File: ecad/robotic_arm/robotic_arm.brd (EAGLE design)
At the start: 81.3 x 61 mm, 118 parts, among them J1 (ID,OD)=(2.1,5.5)MM, SW1 5A/28V, Y1 16MHz

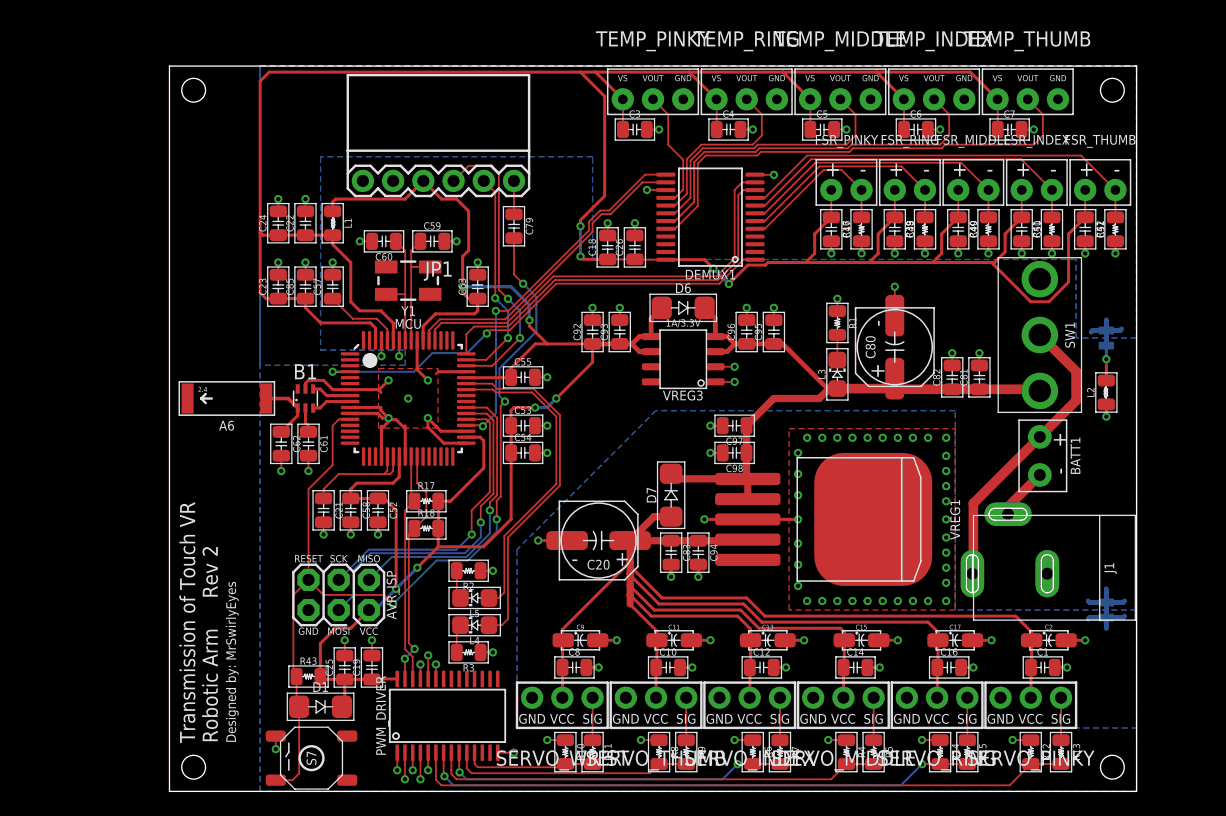
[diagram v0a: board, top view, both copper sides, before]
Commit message: Replaced Robotic Arm components for those with 3D models.  Also went down to 0402 component size.
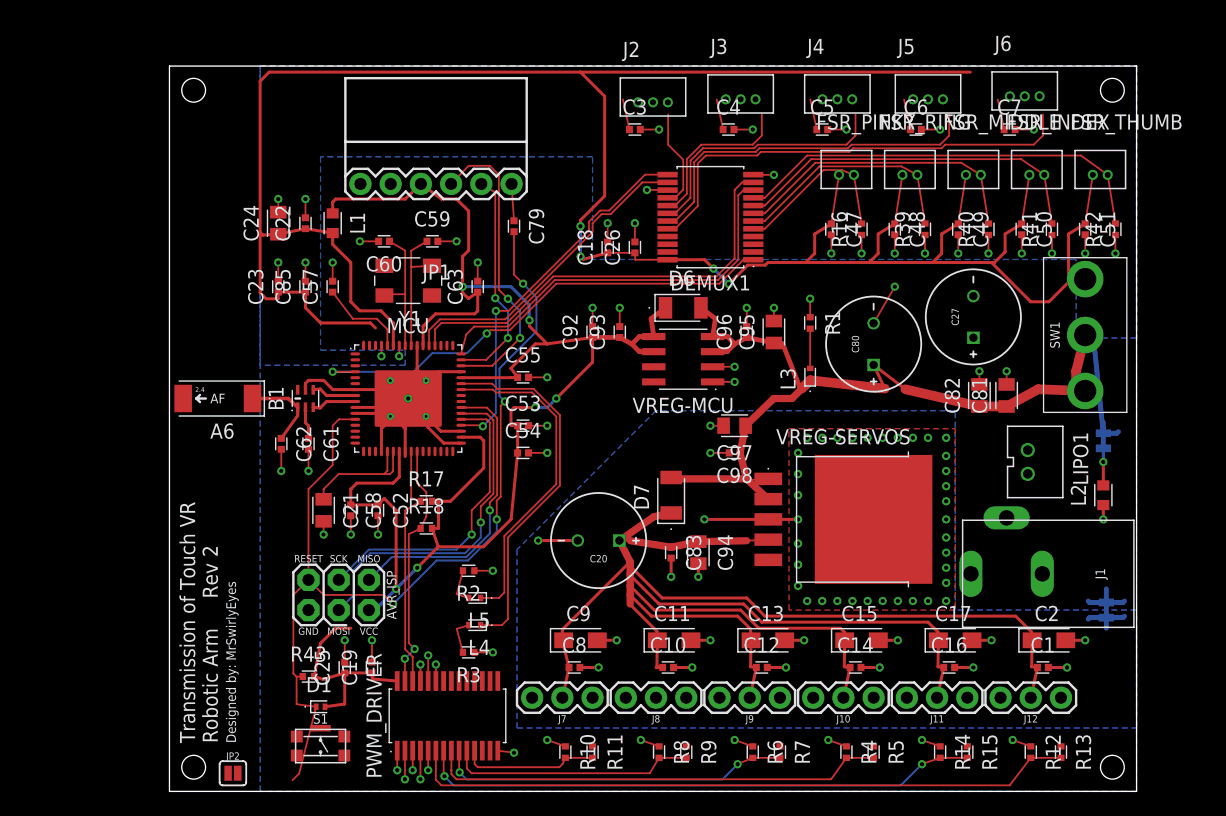
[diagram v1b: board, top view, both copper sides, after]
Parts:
- removed BATT1: BATTERYPTH_HOLES, PiB:DUAL_PTH_PADS
- removed S7: TACTILE-SW_500mA/12V, PiB_switches:BTN_MOMENTARY_SPST-NO_SMD_12V_50MA_L5.2-W5.2
- removed SERVO_INDEX, SERVO_MIDDLE, SERVO_PINKY, SERVO_RING, SERVO_THUMB, SERVO_WRIST: HK15298B, PiB:CONNECTOR_SERVO
- removed TEMP_INDEX, TEMP_MIDDLE, TEMP_PINKY, TEMP_RING, TEMP_THUMB: TMP36, PiB:CONNECTOR_TMP36
- removed VREG1: 5A/5V, PiB_ic_power:TO-263-5
- removed VREG3: 1A/3.3V, PiB_ic_power:SOIC-8_W3.9MM
- added C27: 1000uF/16V, PiB_capacitors:_AE_PTH_DIA8-LS3.5-H21.50
- added J10, J11, J12, J7, J8, J9: HK15298B, PiB_motors:1X03-VERT-MALE
- added J2, J3, J4, J5, J6: (no value), PiB_connectors:_MOLEX-0530470310_VERT_PITCH-1.25MM
- added JP2: JUMPER-SMT_2_NO_SILK, PiB_connectors:SMT-JUMPER_2_NO_SILK
- added LIPO1: Molex VERT 2mm pitch, PiB_batteries:BATTERY_MOLEX-89400_VERT_PITCH-2MM
- added S1: 50mA/32V, PiB_switches:BTN_MOMENTARY_SPDT-NO_L4.6-W2.8
- added VREG-MCU: 1A/3.3V, PiB_ic_power:SOIC127P600X265-8
- added VREG-SERVOS: 5A/5V, PiB_ic_power:TO170P1363X457-6
- A6: value 2.4GHz/802.11/0.5dBi/3W -> 2.45GHz; device PiB_radio_frequency:ANTENNA-CHIP5 -> PiB_radio_frequency:ANTC6522X100
- AVR_ISP: value AVR ISP -> AVRISP
- B1: value Impedence UNBAL/BAL (50Ω/100Ω) -> 50/100; device PiB_radio_frequency:0805_BALUN -> PiB_radio_frequency:RESCAXE65P200X125X95-6
- C1, C10, C12, C14, C16, C19, C22, C23, C26, C3, C4, C47, C48, C49, C5, C50, C51, C52, C53, C54, C55, C57, C58, C6, C63, C7, C79, C8, C83, C85, C93, C96, C98: device PiB_capacitors:_CER_SMD-805 -> PiB_capacitors:CAPC1005X55_SMD-0402
- C11, C13, C15, C17, C2, C9: value 10uF/20V -> 10uF/16V; device PiB_capacitors:_TANT_SMD-1206 -> PiB_capacitors:CAPMP3216X180_SMD_CAP-TANT-1206
- C18, C25, C92: value 10uF/25V -> 10uF/6.3V; device PiB_capacitors:_CER_SMD-805 -> PiB_capacitors:CAPC1005X55_SMD-0402
- C20: value 100UF/16V -> 1000uF/16V; device PiB_capacitors:_AE_SMD_L6.6-W6.6 -> PiB_capacitors:_AE_PTH_DIA8-LS3.5-H21.50
- C21, C24, C82, C94, C95, C97: device PiB_capacitors:_CER_SMD-805 -> PiB_capacitors:CAPC2012X95_SMD-0805
- C59, C60: value 12pF/250V -> 12pF/100V; device PiB_capacitors:_CER_SMD-805 -> PiB_capacitors:CAPC1005X55_SMD-0402
- C61: value 22PF/250V -> 22pF/100V; device PiB_capacitors:_CER_SMD-805 -> PiB_capacitors:CAPC1005X55_SMD-0402
- C62: value 0.75PF/100V -> 0.75pF/50V; device PiB_capacitors:_CER_SMD-805 -> PiB_capacitors:CAPC1005X55_SMD-0402
- C80: value 220uF/16V -> 1000uF/16V; device PiB_capacitors:_AE_SMD_L6.6-W6.6 -> PiB_capacitors:_AE_PTH_DIA8-LS3.5-H21.50
- C81: value 0.1uF/50V -> 0.1uF/35V; device PiB_capacitors:_CER_SMD-805 -> PiB_capacitors:CAPC2012X95_SMD-0805
- D1: value 1A/50V -> 150mA/75V; device PiB_discrete_semiconductors:SOD123F -> PiB_discrete_semiconductors:DFN100X60X55-2
- D6, D7: device PiB_discrete_semiconductors:SOD123F -> PiB_discrete_semiconductors:SODFL3516X170
- DEMUX1: device PiB:SSOP-24 -> PiB:SOP65P780X200-24
- FSR_INDEX, FSR_MIDDLE, FSR_PINKY, FSR_RING, FSR_THUMB: value FSR -> 10K; device PiB:CONNECTOR_FSR -> PiB_sensors:_MOLEX-0530470210_VERT_PITCH-1.25MM
- J1: value (ID,OD)=(2.1,5.5)MM -> 5A/28V; device PiB_connectors:POWER_JACK_SLOT_ID2.1MM-OD5.5MM -> PiB_connectors:POWER_JACK_PTH_ID2.1MM-OD5.5MM
- JP1: value FTDIPTH-RA -> FTDI
- L1, L2: value 10uH -> 10uH/380mA; device PiB_inductors:_SMD-805 -> PiB_inductors:INDC1608X60
- L3, L4, L5: device PiB_leds:LED_SMD-805_ -> PiB_leds:LEDC1005X40
- MCU: value ATMEGA128RFA1 -> ATMEGA128RFA1_VFQFN-64_NO-EXPOSED-PAD; device PiB_ic_microcontrollers:VFQFN-64 -> PiB_ic_microcontrollers:QFN50P900X900X90-64
- PWM_DRIVER: device PiB:TSSOP-28 -> PiB:SOP65P650X110-28
- R1, R10, R12, R14, R16, R39, R4, R40, R41, R42, R43, R6, R8: value 10KΩ -> 10K; device PiB_resistors:RESISTOR_SMD-805 -> PiB_resistors:RESC1005X35_SMD-0402
- R11, R13, R15, R5, R7, R9: value 100Ω -> 100; device PiB_resistors:RESISTOR_SMD-805 -> PiB_resistors:RESC1005X35_SMD-0402
- R17, R18: value 4.7K -> 10K; device PiB_resistors:RESISTOR_SMD-805 -> PiB_resistors:RESC1005X35_SMD-0402
- R2: value 2KΩ -> 1K; device PiB_resistors:RESISTOR_SMD-805 -> PiB_resistors:RESC1005X35_SMD-0402
- R3: value 1KΩ -> 1K; device PiB_resistors:RESISTOR_SMD-805 -> PiB_resistors:RESC1005X35_SMD-0402
- Y1: value 16MHz -> 16 MHz; device PiB:CRYSTAL-SMD-5X3 -> PiB:OSCCC500X320X110
- moved ANALOG_BR 8.64 mm to (81.0, 26.9)
- moved L2 8.64 mm to (81.0, 22.4)
- moved JP1 6.61 mm to (24.9, 48.5), turned to 90 degrees
- moved SW1 3.81 mm to (79.5, 35.8), turned to 0 degrees
- moved J1 3.34 mm to (72.9, 15.7)
- moved C81 2.75 mm to (72.9, 30.7)
- moved C82 2.75 mm to (70.6, 30.7)
- moved L3 2.29 mm to (56.4, 32.5)
- moved R1 2.29 mm to (56.4, 36.8)
- moved C80 1.80 mm to (61.7, 35.1)
- moved A6 0.76 mm to (6.60, 30.5)
- turned B1 to 90 degrees
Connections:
- removed net BATT_+: BATT1.+, J1.PWR, SW1.2
- removed net BATT_-: BATT1.-, J1.GND@2
- new net +: J1.PWR, LIPO1.+, SW1.P
- new net -: J1.GND@1, LIPO1.-
- new net N$12: JP2.2, MCU.62
- net 5V: now also C11.A, C13.A, C15.A, C17.A, C2.A, C20.+, C9.A, J10.VCC, J11.VCC, J12.VCC, J7.VCC, J8.VCC, J9.VCC, VREG-SERVOS.4; no longer C11.+, C13.+, C15.+, C17.+, C2.+, C20.A, C9.+, SERVO_INDEX.2, SERVO_MIDDLE.2, SERVO_PINKY.2, SERVO_RING.2, SERVO_THUMB.2, SERVO_WRIST.2, VREG1.4
- net AGND: now also J2.1, J3.1, J4.1, J5.1, J6.1, MCU.EP, MCU.P$1, MCU.P$2, MCU.P$3, MCU.P$4, MCU.P$5; no longer TEMP_INDEX.3, TEMP_MIDDLE.3, TEMP_PINKY.3, TEMP_RING.3, TEMP_THUMB.3
- net AVCC: now also FSR_INDEX.1, FSR_MIDDLE.1, FSR_PINKY.1, FSR_RING.1, FSR_THUMB.1, J2.3, J3.3, J4.3, J5.3, J6.3, JP2.1; no longer FSR_INDEX.+, FSR_MIDDLE.+, FSR_PINKY.+, FSR_RING.+, FSR_THUMB.+, MCU.62, TEMP_INDEX.1, TEMP_MIDDLE.1, TEMP_PINKY.1, TEMP_RING.1, TEMP_THUMB.1
- net FSR_INDEX: now also FSR_RING.2; no longer FSR_RING.-
- net FSR_MIDDLE: now also FSR_MIDDLE.2; no longer FSR_MIDDLE.-
- net FSR_PINKY: now also FSR_THUMB.2; no longer FSR_THUMB.-
- net FSR_RING: now also FSR_INDEX.2; no longer FSR_INDEX.-
- net FSR_THUMB: now also FSR_PINKY.2; no longer FSR_PINKY.-
- net GND: now also AVR_ISP.GND, C27.-, C80.-, J1.GND@2, S1.2, VREG-MCU.1, VREG-MCU.2; no longer AVR_ISP.6, C80.K, J1.GND@1, S7.1, VREG3.1, VREG3.2
- net MISO: now also AVR_ISP.MISO; no longer AVR_ISP.1
- net MOSI: now also AVR_ISP.MOSI; no longer AVR_ISP.4
- net N$1: now also J7.SIG; no longer SERVO_WRIST.1
- net N$39: now also A6.1; no longer A6.FEED
- net N$4: now also J8.SIG; no longer SERVO_THUMB.1
- net N$6: now also J9.SIG; no longer SERVO_INDEX.1
- net N$7: now also J10.SIG; no longer SERVO_MIDDLE.1
- net N$8: now also J11.SIG; no longer SERVO_RING.1
- net N$9: now also J12.SIG; no longer SERVO_PINKY.1
- net NGND: now also C11.K, C13.K, C15.K, C17.K, C2.K, C20.-, C9.K, J10.GND, J11.GND, J12.GND, J7.GND, J8.GND, J9.GND, VREG-SERVOS.3, VREG-SERVOS.6; no longer C11.-, C13.-, C15.-, C17.-, C2.-, C20.K, C9.-, SERVO_INDEX.3, SERVO_MIDDLE.3, SERVO_PINKY.3, SERVO_RING.3, SERVO_THUMB.3, SERVO_WRIST.3, VREG1.3, VREG1.TAB
- net RESET: now also AVR_ISP.RESET, S1.3; no longer AVR_ISP.5, S7.3
- net SCK: now also AVR_ISP.SCK; no longer AVR_ISP.3
- net TEMP_INDEX: now also J3.2; no longer TEMP_RING.2
- net TEMP_MIDDLE: now also J4.2; no longer TEMP_MIDDLE.2
- net TEMP_PINKY: now also J6.2; no longer TEMP_THUMB.2
- net TEMP_RING: now also J5.2; no longer TEMP_INDEX.2
- net TEMP_THUMB: now also J2.2; no longer TEMP_PINKY.2
- net VBATT: now also C27.+, C80.+, SW1.S1, VREG-MCU.3, VREG-MCU.4, VREG-SERVOS.1, VREG-SERVOS.2; no longer C80.A, SW1.1, VREG1.1, VREG1.2, VREG3.3, VREG3.4
- net VCC: now also VREG-MCU.5, VREG-MCU.6; no longer AVR_ISP.2, VREG3.5, VREG3.6
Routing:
- net BATT_+: track 24.9 -> 0.00 mm
- net AGND: track 31.0 -> 48.8 mm
- net GND: track 99.3 -> 109.7 mm, vias 48 -> 43
- net VBATT: track 56.3 -> 66.3 mm
- net VCC: track 144.0 -> 151.3 mm
- net AVCC: track 235.9 -> 228.8 mm
- net +: track 0.00 -> 5.61 mm
- net NGND: track 34.3 -> 39.9 mm
- net BATT_-: track 4.40 -> 0.00 mm
- net 5V: track 159.8 -> 163.7 mm
- net N$9: track 3.57 -> 0.00 mm
- net N$8: track 3.57 -> 0.00 mm
- net N$7: track 3.57 -> 0.00 mm
- net N$6: track 3.57 -> 0.00 mm
- net N$4: track 3.57 -> 0.00 mm
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- removed copper zone on layer 1, net GND

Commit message: Start on Rev 2 of robotic arm.  Made minor fixes to Touch Glove Rev 2.
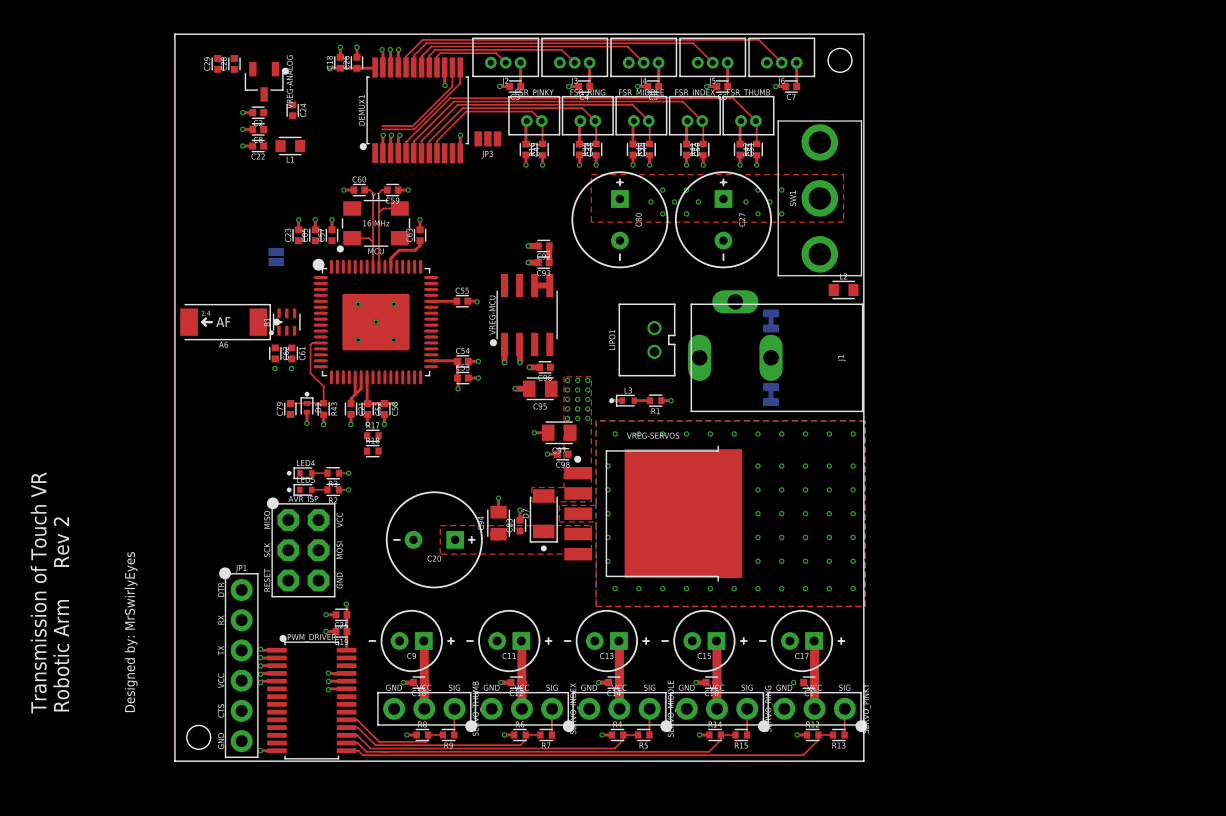
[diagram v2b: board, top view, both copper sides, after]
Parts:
- removed ANALOG_BR: 2PT_GND_TIE, PiB_power_symbols:2PT_GND_TIE
- removed C81: 0.1uF/35V, PiB_capacitors:CAPC2012X95_SMD-0805
- removed C82: 10uF/25V, PiB_capacitors:CAPC2012X95_SMD-0805
- removed D6: 1A/50V, PiB_discrete_semiconductors:SODFL3516X170
- removed J10, J11, J12, J7, J8, J9: HK15298B, PiB_motors:1X03-VERT-MALE
- removed L4: GREEN, PiB_leds:LEDC1005X40
- removed L5: RED, PiB_leds:LEDC1005X40
- removed R10: 10K, PiB_resistors:RESC1005X35_SMD-0402
- removed R11: 100, PiB_resistors:RESC1005X35_SMD-0402
- removed S1: 50mA/32V, PiB_switches:BTN_MOMENTARY_SPDT-NO_L4.6-W2.8
- added C28: 0.1uF/50V, PiB_capacitors:CAPC1005X55_SMD-0402
- added C29: 10uF/6.3V, PiB_capacitors:CAPC1005X55_SMD-0402
- added JP3: JUMPER_SMD_3-PAD_NO_NO-SILK, PiB_connectors:SMT-JUMPER_3_NO_NO-SILK
- added LED4: GREEN, PiB_leds:LEDC1005X40_LED-0402
- added LED5: RED, PiB_leds:LEDC1005X40_LED-0402
- added NOISE_BR1: NET_BRIDGE, PiB_power_symbols:NET_BRIDGE
- added SERVO_INDEX, SERVO_MIDDLE, SERVO_PINKY, SERVO_RING, SERVO_THUMB: HK15298B, PiB_motors:HDRV3W64P254_1X3_762X254X838B
- added VREG-ANALOG: MCP1700-1802 1.8V/200mA, PiB_ic_power:SOT95P237X112-3_SOT-23-3
- AVR_ISP: value AVRISP -> PTH VERT MALE; device PiB_connectors:2X3-NS -> PiB_connectors:HDRV6W64P254_2X3_762X483X838B_AVR-ISP
- C11, C13, C15, C17, C9: value 10uF/16V -> (none); device PiB_capacitors:CAPMP3216X180_SMD_CAP-TANT-1206 -> PiB_capacitors:_AE_PTH-DIA5-LS2-H11
- C2: value 10uF/16V -> 0.1uF/50V; device PiB_capacitors:CAPMP3216X180_SMD_CAP-TANT-1206 -> PiB_capacitors:CAPC1005X55_SMD-0402
- C21: device PiB_capacitors:CAPC2012X95_SMD-0805 -> PiB_capacitors:CAPC1005X55_SMD-0402
- C24: value 1uF/25V -> 0.1uF/50V; device PiB_capacitors:CAPC2012X95_SMD-0805 -> PiB_capacitors:CAPC1005X55_SMD-0402
- C8: value 0.1uF/50V -> 10uF/6.3V
- JP1: device PiB_connectors:FTDI_BASIC-6PIN-MALE-RA -> PiB_connectors:HDRV6W64P254_1X6_1524X254X838B_FTDI
- JP2: value JUMPER-SMT_2_NO_SILK -> JUMPER_SMD_2-PAD_NO_SILK
- L1, L2: device PiB_inductors:INDC1608X60 -> PiB_inductors:INDC1608X60-0603
- L3: device PiB_leds:LEDC1005X40 -> PiB_leds:LEDC1005X40_LED-0402
- LIPO1: value Molex VERT 2mm pitch -> 7.4V
- MCU: value ATMEGA128RFA1_VFQFN-64_NO-EXPOSED-PAD -> ATMEGA128RFA1
- NOISE_BR: value 2PT_GND_TIE -> NET_BRIDGE; device PiB_power_symbols:2PT_GND_TIE -> PiB_power_symbols:NET_BRIDGE
- Y1: device PiB:OSCCC500X320X110 -> PiB_crystals_oscillators_resonators:OSCCC500X320X110_CRYSTAL
- moved C2 79.9 mm to (10.0, 54.5), turned to 180 degrees
- moved C8 52.5 mm to (10.0, 53.1), turned to 180 degrees
- moved JP2 43.5 mm to (11.5, 42.4), flipped to the bottom, turned to 270 degrees
- moved JP1 37.8 mm to (8.61, 14.4), turned to 270 degrees
- moved NOISE_BR 33.5 mm to (53.1, 30.8)
- moved LIPO1 33.0 mm to (43.3, 35.4), turned to 90 degrees
- moved R42 30.9 mm to (51.9, 51.4)
- moved R41 30.1 mm to (47.4, 51.4)
- moved FSR_THUMB 29.9 mm to (51.2, 53.8)
- moved C51 29.8 mm to (50.5, 51.4)
- moved R40 29.3 mm to (42.9, 51.4)
- moved J1 29.1 mm to (50.1, 33.9)
- moved FSR_INDEX 29.1 mm to (46.7, 53.8)
- moved C50 29.0 mm to (46.0, 51.4)
- moved R39 28.4 mm to (38.4, 51.4)
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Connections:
- removed net C10: DEMUX1.21
- removed net C5: DEMUX1.4
- removed net C6: DEMUX1.3
- removed net C7: DEMUX1.2
- removed net C8: DEMUX1.23
- removed net C9: DEMUX1.22
- removed net N$38: ANALOG_BR.P$1, L2.2
- removed net PWM10: PWM_DRIVER.17
- removed net PWM11: PWM_DRIVER.18
- removed net PWM12: PWM_DRIVER.19
- removed net PWM13: PWM_DRIVER.20
- removed net PWM14: PWM_DRIVER.21
- removed net PWM15: PWM_DRIVER.22
- removed net PWM6: PWM_DRIVER.12
- removed net PWM7: PWM_DRIVER.13
- removed net PWM8: PWM_DRIVER.15
- removed net PWM9: PWM_DRIVER.16
- removed net SERVO_WRIST: PWM_DRIVER.11, R10.2, R11.2
- removed net VBATT: C27.+, C80.+, C81.1, C82.1, C95.1, C96.1, C97.1, C98.1, D6.K, D7.K, L3.A, SW1.S1, VREG-MCU.3, VREG-MCU.4, VREG-SERVOS.1, VREG-SERVOS.2
- new net 3.3V: C19.1, C24.1, C25.1, C52.1, C53.1, C54.1, C55.1, C58.1, C63.1, C92.1, C93.1, D1.K, L1.1, MCU.23, MCU.34, MCU.44, MCU.54, PWM_DRIVER.28, R17.2, R18.2, R43.2, VREG-MCU.5, VREG-MCU.6
- new net A1.8V: C28.1, C29.1, JP3.1, VREG-ANALOG.2
- new net A3.3V: C18.1, C2.1, C22.1, C26.1, C3.1, C4.1, C5.1, C6.1, C7.1, C8.1, DEMUX1.24, J2.3, J3.3, J4.3, J5.3, J6.3, JP3.3, L1.2, VREG-ANALOG.3
- new net VBAT: C27.+, C80.+, C95.1, C96.1, C97.1, C98.1, D7.K, L3.A, SW1.P, VREG-MCU.3, VREG-MCU.4, VREG-SERVOS.1, VREG-SERVOS.2
- new net VSENSOR: C47.1, C48.1, C49.1, C50.1, C51.1, FSR_INDEX.1, FSR_MIDDLE.1, FSR_PINKY.1, FSR_RING.1, FSR_THUMB.1, JP3.2
- net +: now also SW1.S1; no longer SW1.P
- net -: now also J1.GND_BATTERY; no longer J1.GND@1
- net 5V: now also C11.+, C13.+, C15.+, C17.+, C9.+, SERVO_INDEX.VCC, SERVO_MIDDLE.VCC, SERVO_PINKY.VCC, SERVO_RING.VCC, SERVO_THUMB.VCC; no longer C11.A, C13.A, C15.A, C17.A, C2.A, C8.1, C9.A, J10.VCC, J11.VCC, J12.VCC, J7.VCC, J8.VCC, J9.VCC
- net AGND: now also B1.5, C2.2, C28.2, C29.2, C61.2, C62.2, C8.2, DEMUX1.2, DEMUX1.21, DEMUX1.22, DEMUX1.23, DEMUX1.3, DEMUX1.4, L2.2, MCU.10, MCU.7, VREG-ANALOG.1; no longer ANALOG_BR.P$2
- net AVCC: no longer C18.1, C22.1, C24.1, C26.1, C3.1, C4.1, C47.1, C48.1, C49.1, C5.1, C50.1, C51.1, C6.1, C7.1, DEMUX1.24, FSR_INDEX.1, FSR_MIDDLE.1, FSR_PINKY.1, FSR_RING.1, FSR_THUMB.1, J2.3, J3.3, J4.3, J5.3, J6.3, L1.2
- net FSR_INDEX: now also DEMUX1.8; no longer DEMUX1.6
- net FSR_PINKY: now also DEMUX1.5; no longer DEMUX1.9
- net FSR_RING: now also DEMUX1.6; no longer DEMUX1.8
- net FSR_THUMB: now also DEMUX1.9; no longer DEMUX1.5
- net GND: now also C59.1, C60.1, J1.GND_JACK, NOISE_BR1.P$1; no longer B1.5, C59.2, C60.2, C61.2, C62.2, C81.2, C82.2, J1.GND@2, L2.1, MCU.10, MCU.7, R10.1, S1.2
- net N$1: now also L2.1, NOISE_BR1.P$2; no longer J7.SIG, R11.1
- net N$3: now also LED4.K; no longer L4.K
- net N$30: now also C60.2, Y1.1; no longer C60.1, Y1.3
- net N$35: now also C59.2, Y1.3; no longer C59.1, Y1.1
- net N$4: now also SERVO_THUMB.SIG; no longer J8.SIG
- net N$5: now also LED5.K; no longer L5.K
- net N$6: now also SERVO_INDEX.SIG; no longer J9.SIG
- net N$7: now also SERVO_MIDDLE.SIG; no longer J10.SIG
- net N$8: now also SERVO_RING.SIG; no longer J11.SIG
- net N$9: now also SERVO_PINKY.SIG; no longer J12.SIG
- net NGND: now also C11.-, C13.-, C15.-, C17.-, C9.-, SERVO_INDEX.GND, SERVO_MIDDLE.GND, SERVO_PINKY.GND, SERVO_RING.GND, SERVO_THUMB.GND, VREG-SERVOS.TAB; no longer C11.K, C13.K, C15.K, C17.K, C2.K, C8.2, C9.K, J10.GND, J11.GND, J12.GND, J7.GND, J8.GND, J9.GND, VREG-SERVOS.6
- net PB6: now also LED5.A; no longer L5.A
- net PB7: now also LED4.A; no longer L4.A
- net RESET: no longer S1.3
- net RX0: now also JP1.TX; no longer JP1.TXO
- net SERVO_INDEX: now also PWM_DRIVER.18; no longer PWM_DRIVER.9
- net SERVO_MIDDLE: now also PWM_DRIVER.17; no longer PWM_DRIVER.8
- net SERVO_PINKY: now also PWM_DRIVER.15; no longer PWM_DRIVER.6
- net SERVO_RING: now also PWM_DRIVER.16; no longer PWM_DRIVER.7
- net SERVO_THUMB: now also PWM_DRIVER.19; no longer PWM_DRIVER.10
- net TX0: now also JP1.RX; no longer JP1.RXI
- net VCC: no longer C19.1, C25.1, C52.1, C53.1, C54.1, C55.1, C58.1, C63.1, C92.1, C93.1, D1.K, D6.A, L1.1, MCU.23, MCU.34, MCU.44, MCU.54, PWM_DRIVER.28, R17.2, R18.2, R43.2, VREG-MCU.5, VREG-MCU.6
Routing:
- net AVCC: track 228.8 -> 0.00 mm, vias 4 -> 0
- net VCC: track 151.3 -> 0.00 mm, vias 6 -> 0
- net 5V: track 163.7 -> 29.0 mm
- net RESET: track 82.7 -> 9.10 mm, vias 4 -> 0
- net GND: track 109.7 -> 36.4 mm, vias 43 -> 35
- net VBATT: track 66.3 -> 0.00 mm
- net A5: track 43.5 -> 0.00 mm, vias 2 -> 0
- net PE6: track 36.6 -> 0.00 mm
- net PE2: track 34.0 -> 0.00 mm
- net NGND: track 39.9 -> 7.41 mm, vias 54 -> 61
- net PB7: track 30.9 -> 0.00 mm
- net MOSI: track 28.9 -> 0.00 mm, vias 1 -> 0
- net PB6: track 27.7 -> 0.00 mm
- net RX0: track 25.3 -> 0.00 mm, vias 2 -> 0
- net SCK: track 25.3 -> 0.00 mm, vias 1 -> 0
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- added copper zone on layer 15, net 3.3V
- added copper zone on layer 1, net 5V
- added copper zone on layer 15, net 5V
- added copper zone on layer 2, net AGND
- added copper zone on layer 15, net GARBAGE
- added copper zone on layer 2, net GARBAGE
- added copper zone on layer 2, net GND
- added copper zone on layer 15, net NGND
- added copper zone on layer 2, net NGND
- added copper zone on layer 1, net VBAT
- added copper zone on layer 15, net VBAT
- removed copper zone on layer 16, net AGND
- removed copper zone on layer 16, net GND
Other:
- board size 81.3 x 61 mm -> 57.9 x 61.1 mm
